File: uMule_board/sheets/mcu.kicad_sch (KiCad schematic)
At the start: 29 parts, among them SW1 DBG_BUTT, SW2 RST, U6 STM32F103RCTx, U7 FM24C64B, Y1 8MHz

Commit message: initial commit for new processor. Need to adjust pinout and layout of board. Try not to change elements names to save DC converters and photodiodes layout
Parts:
- added U17: STM32G474RETx, Package_QFP:LQFP-64_10x10mm_P0.5mm, symbol MCU_ST_STM32G4:STM32G474RETx
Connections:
- new net: U17.15 (VSS), U17.31 (VSS), U17.47 (VSS), U17.63 (VSS)
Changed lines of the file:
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@@
 		)
 	)
-	(text_box "Dodać jakieś ledy do debugu (chociaż 3)\n\nDodać wyjścia na czujniki(Wszystkie pozostałe wyjścia na goldpiny)\r\n"
+	(text_box "Dodać więcej kondensatorów, spróbować przenieść piny na lepszą STMkę"
 		(exclude_from_sim no)
 		(at 13.97 13.97 0)
 		(size 76.2 24.13)
+		(margins 0.9525 0.9525 0.9525 0.9525)
+		(stroke
+			(width 0)
+			(type solid)
+		)
+		(fill
+			(type none)
+		)
+		(effects
+			(font
+				(size 1.27 1.27)
+			)
+			(justify left top)
+		)
+	)
+	(text_box "New cortex (STM32G474RET6) :\nhttps://www.google.com/url?sa=t&source=web&rct=j&opi=89978449&url=https://www.st.com/resource/en/datasheet/stm32g474cb.pdf&ved=2ahUKEwjkoOWv1-KRAxXXKRAIHbOCAG0QFnoECB8QAQ&usg=AOvVaw3OZEQOb27mfL1C1gOsxmsy"
+		(exclude_from_sim no)
+		(at 207.01 129.54 0)
+		(size 57.15 11.43)
 		(margins 0.9525 0.9525 0.9525 0.9525)
 		(stroke
@@
 					(unit 1)
 				)
+			)
+		)
+	)
+	(symbol
+		(lib_id "MCU_ST_STM32G4:STM32G474RETx")
+		(at 243.84 74.93 0)
+		(unit 1)
+		(exclude_from_sim no)
+		(in_bom yes)
+		(on_board yes)
+		(dnp no)
+		(fields_autoplaced yes)
+		(property "Reference" "U17"
+			(at 248.5233 123.19 0)
+			(effects
+				(font
+					(size 1.27 1.27)
+				)
+				(justify left)
+			)
+		)
+		(property "Value" "STM32G474RETx"
+			(at 248.5233 125.73 0)
+			(effects
+				(font
+					(size 1.27 1.27)
+				)
+				(justify left)
+			)
+		)
+		(property "Footprint" "Package_QFP:LQFP-64_10x10mm_P0.5mm"
+			(at 228.6 120.65 0)
+			(effects
+				(font
+					(size 1.27 1.27)
+				)
+				(justify right)
+				(hide yes)
+			)
+		)
+		(property "Datasheet" "https://www.st.com/resource/en/datasheet/stm32g474re.pdf"
+			(at 243.84 74.93 0)
+			(effects
+				(font
+					(size 1.27 1.27)
+				)
+				(hide yes)
+			)
+		)
+		(property "Description" "STMicroelectronics Arm Cortex-M4 MCU, 512KB flash, 128KB RAM, 170 MHz, 1.71-3.6V, 52 GPIO, LQFP64"
+			(at 243.84 74.93 0)
+			(effects
+				(font
+					(size 1.27 1.27)
+				)
+				(hide yes)
+			)
+		)
+		(pin "54"
+		)
+		(pin "33"
+		)
+		(pin "34"
+		)
+		(pin "24"
+		)
+		(pin "42"
+		)
+		(pin "1"
+		)
+		(pin "39"
+		)
+		(pin "36"
+		)
+		(pin "45"
+		)
+		(pin "25"
+		)
+		(pin "46"
+		)
+		(pin "50"
+		)
+		(pin "20"
+		)
+		(pin "53"
+		)
+		(pin "40"
+		)
+		(pin "19"
+		)
+		(pin "35"
+		)
+		(pin "30"
+		)
+		(pin "59"
+		)
+		(pin "11"
+		)
+		(pin "27"
+		)
+		(pin "14"
+		)
+		(pin "12"
+		)
+		(pin "17"
+		)
+		(pin "63"
+		)
+		(pin "7"
+		)
+		(pin "28"
+		)
+		(pin "37"
+		)
+		(pin "16"
+		)
+		(pin "32"
+		)
+		(pin "41"
+		)
+		(pin "51"
+		)
+		(pin "38"
+		)
+		(pin "2"
+		)
+		(pin "49"
+		)
+		(pin "60"
+		)
+		(pin "21"
+		)
+		(pin "4"
+		)
+		(pin "31"
+		)
+		(pin "18"
+		)
+		(pin "44"
+		)
+		(pin "55"
+		)
+		(pin "6"
+		)
+		(pin "5"
+		)
+		(pin "62"
+		)
+		(pin "15"
+		)
+		(pin "3"
+		)
+		(pin "26"
+		)
+		(pin "58"
+		)
+		(pin "48"
+		)
+		(pin "61"
+		)
+		(pin "29"
+		)
+		(pin "23"
+		)
+		(pin "13"
+		)
+		(pin "22"
+		)
+		(pin "52"
+		)
+		(pin "57"
+		)
+		(pin "47"
+		)
+		(pin "56"
+		)
+		(pin "8"
+		)
+		(pin "9"
+		)
+		(pin "64"
+		)
+		(pin "43"
+		)
+		(pin "10"
+		)
+		(instances
+			(project ""
+				(path "/3d853824-a92e-40a5-ad1a-5052c8a0bd68/fc91144e-0e07-42a9-888c-118bbfe121ea"
+					(reference "U17")
+					(unit 1)
+				)

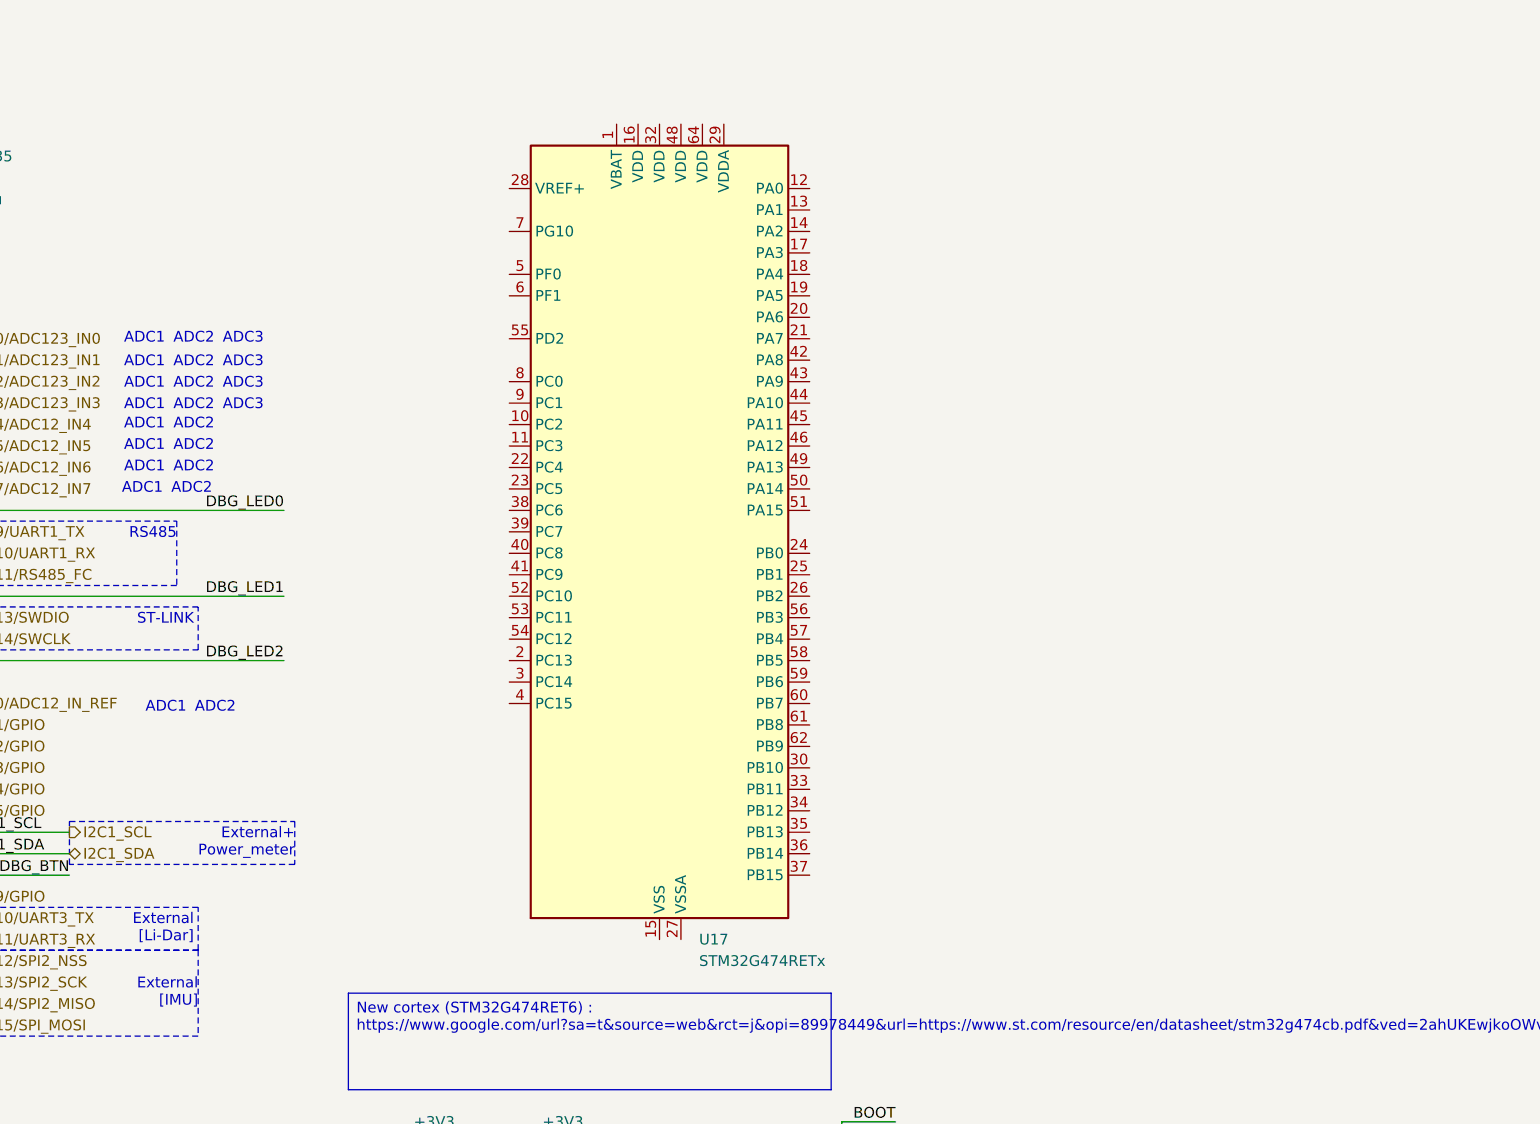
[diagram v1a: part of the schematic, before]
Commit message: Described pinout. Board seems viable
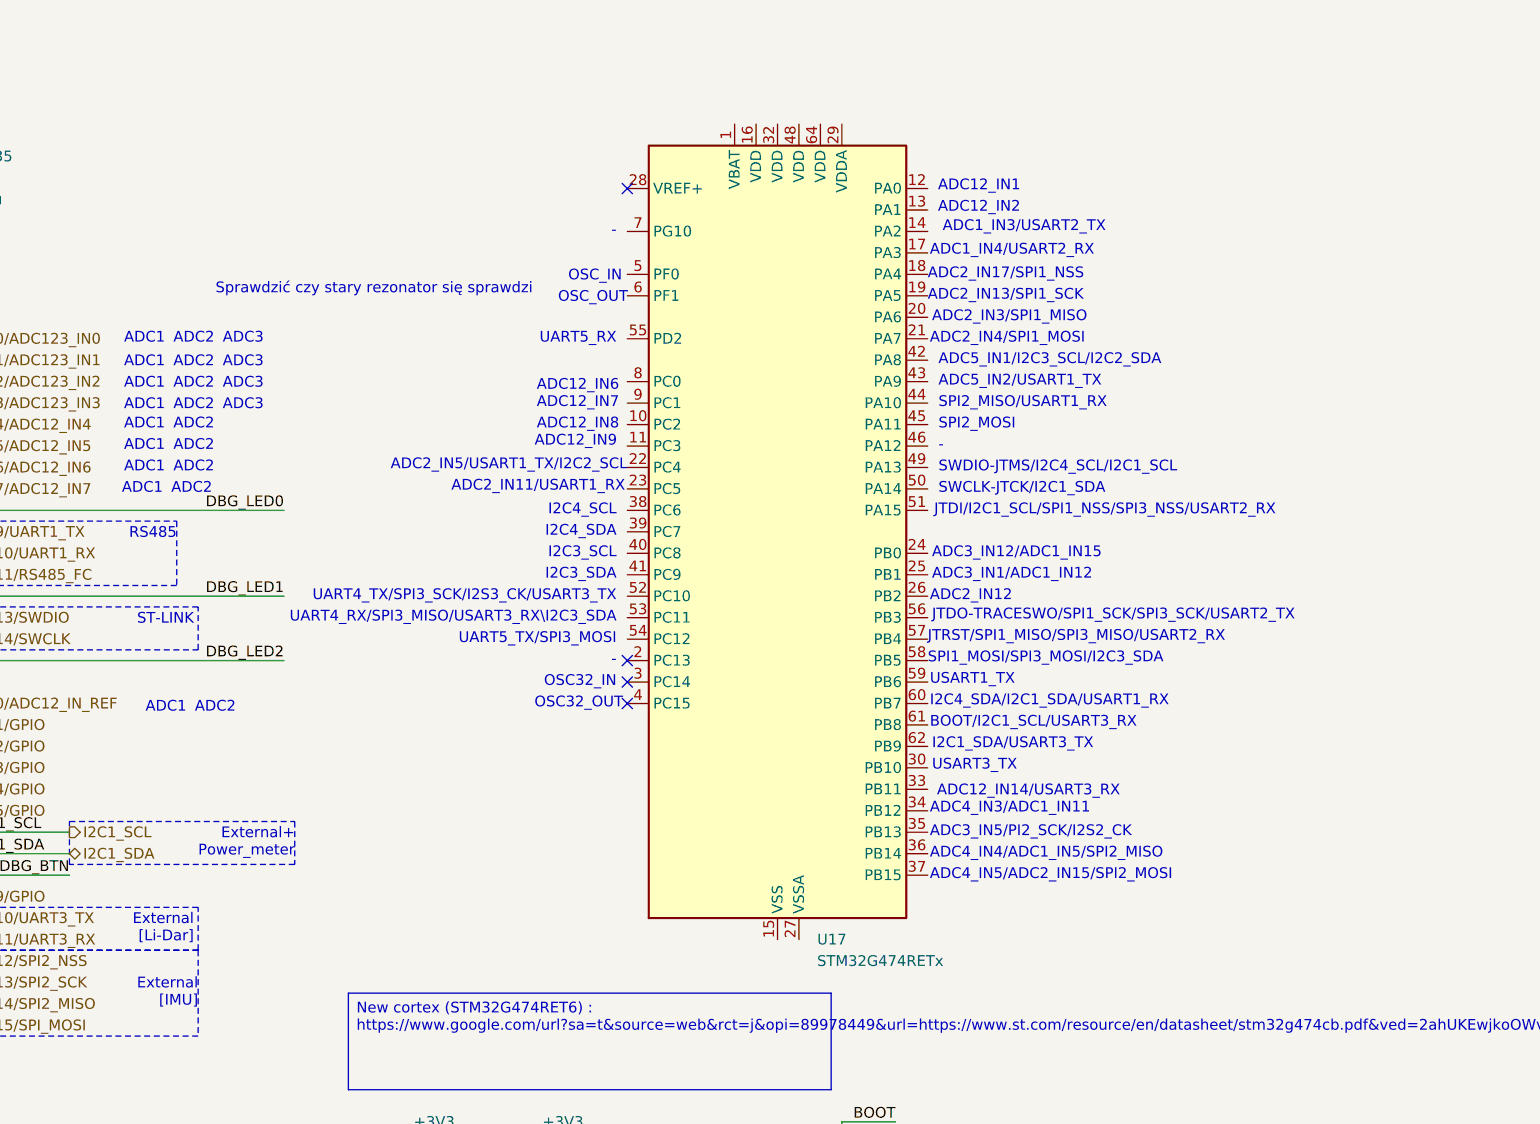
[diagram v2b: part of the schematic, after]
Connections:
- no-connect marks 0 -> 4
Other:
- note added: "-"
- note added: "ADC12_IN1"
- note added: "ADC12_IN14/USART3_RX"
- note added: "ADC12_IN2"
- note added: "ADC12_IN6"
- note added: "ADC12_IN7"
- note added: "ADC12_IN8"
- note added: "ADC12_IN9"
- note added: "ADC1_IN3/USART2_TX"
- note added: "ADC1_IN4/USART2_RX"
- note added: "ADC2_IN11/USART1_RX"
- note added: "ADC2_IN12"
- note added: "ADC2_IN13/SPI1_SCK"
- note added: "ADC2_IN17/SPI1_NSS"
- note added: "ADC2_IN3/SPI1_MISO"
- note added: "ADC2_IN4/SPI1_MOSI"
- note added: "ADC2_IN5/USART1_TX/I2C2_SCL"
- note added: "ADC3_IN1/ADC1_IN12"
- note added: "ADC3_IN12/ADC1_IN15"
- note added: "ADC3_IN5/PI2_SCK/I2S2_CK"
- note added: "ADC4_IN3/ADC1_IN11"
- note added: "ADC4_IN4/ADC1_IN5/SPI2_MISO"
- note added: "ADC4_IN5/ADC2_IN15/SPI2_MOSI"
- note added: "ADC5_IN1/I2C3_SCL/I2C2_SDA"
- note added: "ADC5_IN2/USART1_TX"
- note added: "BOOT/I2C1_SCL/USART3_RX"
- note added: "I2C1_SDA/USART3_TX"
- note added: "I2C3_SCL"
- note added: "I2C3_SDA"
- note added: "I2C4_SCL"
- note added: "I2C4_SDA"
- note added: "I2C4_SDA/I2C1_SDA/USART1_RX"
- note added: "JTDI/I2C1_SCL/SPI1_NSS/SPI3_NSS/USART2_RX"
- note added: "JTDO-TRACESWO/SPI1_SCK/SPI3_SCK/USART2_TX"
- note added: "JTRST/SPI1_MISO/SPI3_MISO/USART2_RX"
- note added: "OSC32_IN"
- note added: "OSC32_OUT"
- note added: "OSC_IN"
- note added: "OSC_OUT"
- note added: "SPI1_MOSI/SPI3_MOSI/I2C3_SDA"
- note added: "SPI2_MISO/USART1_RX"
- note added: "SPI2_MOSI"
- note added: "SWCLK-JTCK/I2C1_SDA"
- note added: "SWDIO-JTMS/I2C4_SCL/I2C1_SCL"
- note added: "Sprawdzić czy stary rezonator się sprawdzi"
- note added: "UART4_RX/SPI3_MISO/USART3_RX\I2C3_SDA"
- note added: "UART4_TX/SPI3_SCK/I2S3_CK/USART3_TX"
- note added: "UART5_RX"
- note added: "UART5_TX/SPI3_MOSI"
- note added: "USART1_TX"
- note added: "USART3_TX"
- moved on the sheet: U17

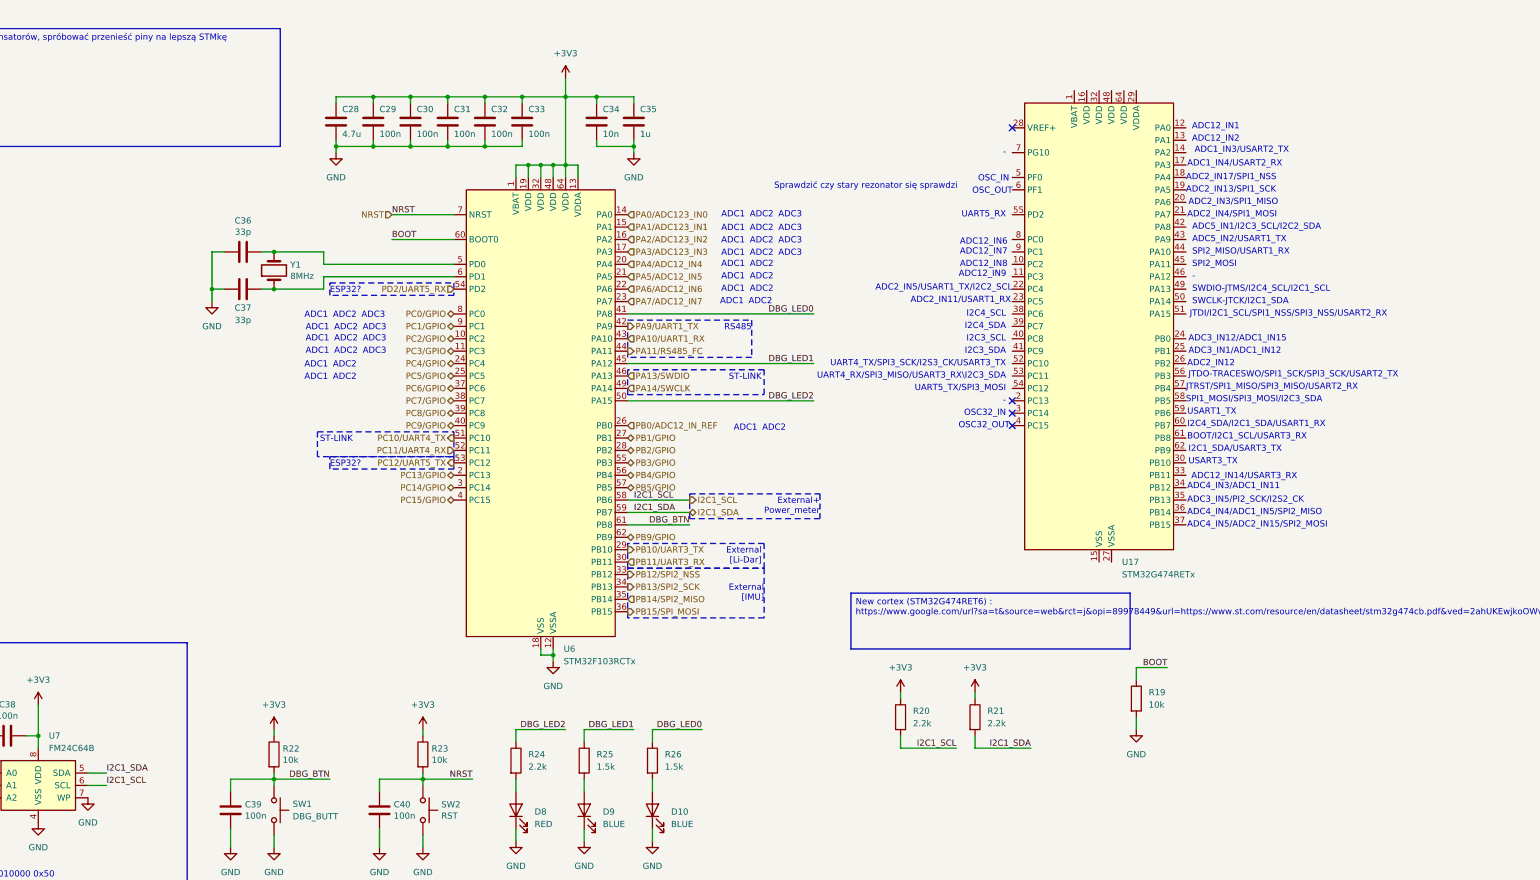
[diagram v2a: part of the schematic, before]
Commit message: initial board is ready for conecting
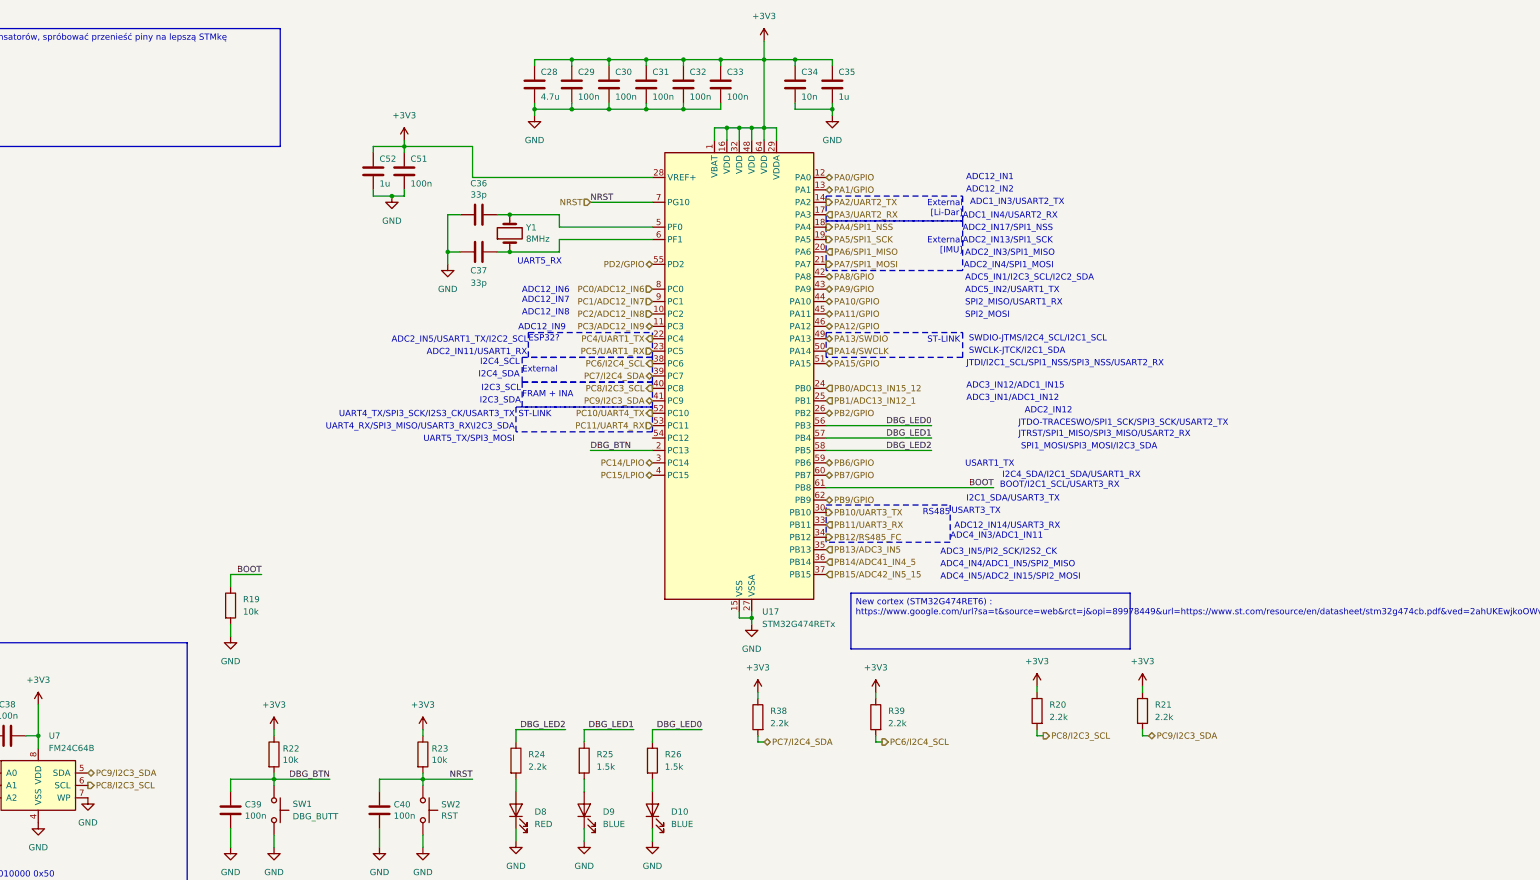
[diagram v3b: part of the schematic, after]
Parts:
- removed U6: STM32F103RCTx, Package_QFP:LQFP-64_10x10mm_P0.5mm, symbol MCU_ST_STM32F1:STM32F103RCTx
- added C51: 100n, Capacitor_SMD:C_0603_1608Metric, symbol Device:C
- added C52: 1u, Capacitor_SMD:C_0603_1608Metric, symbol Device:C
- added R38, R39: 2.2k, Resistor_SMD:R_0603_1608Metric, symbol Device:R
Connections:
- net I2C1_SCL is gone; now on net PC8/I2C3_SCL: R20.2, U7.6 (SCL)
- net I2C1_SDA is gone; now on net PC9/I2C3_SDA: R21.2, U7.5 (SDA)
- net +3V3: now also U17.1 (VBAT), U17.16 (VDD), U17.28 (VREF+), U17.29 (VDDA), U17.32 (VDD), U17.48 (VDD), U17.64 (VDD), C51.1, C52.1, R38.1, R39.1
- net BOOT: now also U17.61 (PB8)
- net DBG_BTN: now also U17.2 (PC13)
- net DBG_LED0: now also U17.56 (PB3)
- net DBG_LED1: now also U17.57 (PB4)
- net DBG_LED2: now also U17.58 (PB5)
- net GND: now also U17.15 (VSS), U17.27 (VSSA), U17.31 (VSS), U17.47 (VSS), U17.63 (VSS), C51.2, C52.2
- net NRST: now also U17.7 (PG10)
- net PA13/SWDIO: now also U17.49 (PA13)
- net PA14/SWCLK: now also U17.50 (PA14)
- net PB10/UART3_TX: now also U17.30 (PB10)
- net PB11/UART3_RX: now also U17.33 (PB11)
- net PB2/GPIO: now also U17.26 (PB2)
- net PB9/GPIO: now also U17.62 (PB9)
- net PC10/UART4_TX: now also U17.52 (PC10)
- net PC11/UART4_RX: now also U17.53 (PC11)
- net at C36.1, Y1.2: now also U17.5 (PF0)
- net PC2/ADC12_IN8: now reaches U17.10 (PC2)
- net PC3/ADC12_IN9: now reaches U17.11 (PC3)
- net PA0/GPIO: now reaches U17.12 (PA0)
- net PA1/GPIO: now reaches U17.13 (PA1)
- net PA2/UART2_TX: now reaches U17.14 (PA2)
- net PA3/UART2_RX: now reaches U17.17 (PA3)
- net PA4/SPI1_NSS: now reaches U17.18 (PA4)
- net PA5/SPI1_SCK: now reaches U17.19 (PA5)
- net PA6/SPI1_MISO: now reaches U17.20 (PA6)
- net PA7/SPI1_MOSI: now reaches U17.21 (PA7)
- net PC4/UART1_TX: now reaches U17.22 (PC4)
- net PC5/UART1_RX: now reaches U17.23 (PC5)
- net PB0/ADC13_IN15_12: now reaches U17.24 (PB0)
- net PB1/ADC13_IN12_1: now reaches U17.25 (PB1)
- net PC14/LPIO: now reaches U17.3 (PC14)
- net PB12/RS485_FC: now reaches U17.34 (PB12)
- net PB13/ADC3_IN5: now reaches U17.35 (PB13)
- net PB14/ADC41_IN4_5: now reaches U17.36 (PB14)
- net PB15/ADC42_IN5_15: now reaches U17.37 (PB15)
- net PC6/I2C4_SCL: now reaches U17.38 (PC6)
- net PC6/I2C4_SCL: now also R39.2
- net PC7/I2C4_SDA: now reaches U17.39 (PC7)
- net PC7/I2C4_SDA: now also R38.2
- net PC15/LPIO: now reaches U17.4 (PC15)
- net PC8/I2C3_SCL: now reaches U17.40 (PC8)
- net PC9/I2C3_SDA: now reaches U17.41 (PC9)
- net PA8/GPIO: now reaches U17.42 (PA8)
- net PA9/GPIO: now reaches U17.43 (PA9)
- net PA10/GPIO: now reaches U17.44 (PA10)
- net PA11/GPIO: now reaches U17.45 (PA11)
- net PA12/GPIO: now reaches U17.46 (PA12)
- net PA15/GPIO: now reaches U17.51 (PA15)
- net PD2/GPIO: now reaches U17.55 (PD2)
- net PB6/GPIO: now reaches U17.59 (PB6)
- net at U17.6 (PF1): now also C37.1, Y1.1
- net PB7/GPIO: now reaches U17.60 (PB7)
- net PC0/ADC12_IN6: now reaches U17.8 (PC0)
- net PC1/ADC12_IN7: now reaches U17.9 (PC1)
- no-connect marks 4 -> 0
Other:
- note added: "External"
- note added: "FRAM + INA"
- note removed: "-"
- note removed: "ADC1"
- note removed: "ADC2"
- note removed: "ADC3"
- note removed: "External+ Power_meter"
- note removed: "OSC32_IN"
- note removed: "OSC32_OUT"
- note removed: "OSC_IN"
- note removed: "OSC_OUT"
- note removed: "Sprawdzić czy stary rezonator się sprawdzi"
- moved on the sheet: R19, R20, R21, U17, Y1
